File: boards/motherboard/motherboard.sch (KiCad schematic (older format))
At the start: 36 parts

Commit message: updates to mother board
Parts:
- 350ma1, 350ma10, 350ma11, 350ma12, 350ma13, 350ma14, 350ma15, 350ma2, 350ma3, 350ma4, 350ma5, 350ma6, 350ma7, 350ma8, 350ma9: renamed from 350ma?; footprint (none) -> lighting:350ma constant current xl4001
- J1, J2, J3, J4, J5: renamed from J?; footprint (none) -> lighting:RJ45
- R1, R10, R11, R12, R13, R14, R15, R2, R3, R4, R5, R6, R7, R8, R9: renamed from R?; footprint (none) -> Resistors_ThroughHole:Resistor_Horizontal_RM10mm
- U1: renamed from U?; footprint (none) -> lighting:pwm_pca9685
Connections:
- net GNDPWR: no longer 350ma14.5 (pwm), 350ma3.5 (pwm), 350ma5.5 (pwm), R14.2, R3.2, R5.2, U1.14 (LED13), U1.3 (LED2), U1.5 (LED4)
- net VCC: now also R11.1; no longer R11.2
- net led0: now also 350ma1.5 (pwm), R1.2
- net led1: no longer 350ma1.5 (pwm), R1.2
- net led10: now also R11.2; no longer R11.1
- new net led13: 350ma14.5 (pwm), R14.2, U1.14 (LED13)
- new net led2: 350ma3.5 (pwm), R3.2, U1.3 (LED2)
- new net led4: 350ma5.5 (pwm), R5.2, U1.5 (LED4)
- no-connect marks 3 -> 18
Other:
- moved on the sheet: 350ma10, 350ma11, 350ma12, 350ma13, 350ma14, 350ma15, 350ma4, 350ma7, 350ma8, 350ma9, J3, J4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

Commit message: mother board pcb
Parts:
- added P1: CONN_01X02, Pin_Headers:Pin_Header_Straight_1x02, symbol CONN_01X02
- added P2, P3: CONN_01X04, Pin_Headers:Pin_Header_Straight_1x04, symbol CONN_01X04
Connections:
- net +24V: now also P1.1 (P1); no longer 350ma9.5 (pwm), R9.2, U1.9 (LED8)
- net GND: now also P2.4 (P4), P3.4 (P4)
- net GNDPWR: now also P1.2 (P2)
- net VCC: now also P2.1 (P1), P3.1 (P1); no longer R12.1
- net sda: now reaches U1.19 (SDA), U1.25 (SDA)
- net sda: now also P2.2 (P2), P3.2 (P2)
- net scl: now reaches U1.20 (SCL), U1.26 (SCL)
- net scl: now also P2.3 (P3), P3.3 (P3)
- new net led8: 350ma9.5 (pwm), R9.2, U1.9 (LED8)
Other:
- moved on the sheet: 350ma1, 350ma10, R10, R12, R2
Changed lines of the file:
@@
 $EndComp
 $Comp
-L +24V #PWR01
+L +24V #PWR1
 U 1 1 5787E774
 P 8600 1350
-F 0 "#PWR01" H 8600 1200 50  0001 C CNN
+F 0 "#PWR1" H 8600 1200 50  0001 C CNN
 F 1 "+24V" H 8600 1490 50  0000 C CNN
 F 2 "" H 8600 1350 50  0000 C CNN
@@
 $EndComp
 $Comp
-L GNDPWR #PWR02
+L GNDPWR #PWR2
 U 1 1 5787E79E
 P 9150 1250
-F 0 "#PWR02" H 9150 1050 50  0001 C CNN
+F 0 "#PWR2" H 9150 1050 50  0001 C CNN
 F 1 "GNDPWR" H 9150 1120 50  0000 C CNN
 F 2 "" H 9150 1200 50  0000 C CNN
@@
 L Led_Driver 350ma1
 U 1 1 5787EC48
-P 5100 1700
-F 0 "350ma1" H 5100 1700 60  0000 C CNN
-F 1 "Led_Driver" H 5150 1800 60  0000 C CNN
-F 2 "lighting:350ma constant current xl4001" H 5100 1700 60  0001 C CNN
-F 3 "" H 5100 1700 60  0000 C CNN
-	1    5100 1700
+P 5050 1700
+F 0 "350ma1" H 5050 1700 60  0000 C CNN
+F 1 "Led_Driver" H 5100 1800 60  0000 C CNN
+F 2 "lighting:350ma constant current xl4001" H 5050 1700 60  0001 C CNN
+F 3 "" H 5050 1700 60  0000 C CNN
+	1    5050 1700
 	1    0    0    -1
 $EndComp
@@
 Text Label 5650 1050 0    60   ~ 0
 vpwr
-Text Label 5600 1200 0    60   ~ 0
-gndpwr
-Text Label 4600 1200 0    60   ~ 0
-vpwr
-Text Label 4600 1500 0    60   ~ 0
+Text Label 5550 1200 0    60   ~ 0
+gndpwr
+Text Label 4550 1200 0    60   ~ 0
+vpwr
+Text Label 4550 1500 0    60   ~ 0
 gnd
 Text Label 5650 1350 0    60   ~ 0
@@
 $EndComp
 $Comp
-L Led_Driver 350ma11
-U 1 1 5787FC55
-P 2600 3850
-F 0 "350ma11" H 2600 3850 60  0000 C CNN
-F 1 "Led_Driver" H 2650 3950 60  0000 C CNN
-F 2 "lighting:350ma constant current xl4001" H 2600 3850 60  0001 C CNN
-F 3 "" H 2600 3850 60  0000 C CNN
-	1    2600 3850
-	1    0    0    -1
-$EndComp
-$Comp
 L Led_Driver 350ma10
 U 1 1 5787FC5B
-P 1550 4000
-F 0 "350ma10" H 1550 4000 60  0000 C CNN
-F 1 "Led_Driver" H 1600 4100 60  0000 C CNN
-F 2 "lighting:350ma constant current xl4001" H 1550 4000 60  0001 C CNN
-F 3 "" H 1550 4000 60  0000 C CNN
-	1    1550 4000
+P 1250 4000
+F 0 "350ma10" H 1250 4000 60  0000 C CNN
+F 1 "Led_Driver" H 1300 4100 60  0000 C CNN
+F 2 "lighting:350ma constant current xl4001" H 1250 4000 60  0001 C CNN
+F 3 "" H 1250 4000 60  0000 C CNN
+	1    1250 4000
 	1    0    0    -1
 $EndComp
@@
 Text Label 2100 3350 0    60   ~ 0
 vpwr
-Text Label 2050 3500 0    60   ~ 0
-gndpwr
-Text Label 1050 3500 0    60   ~ 0
-vpwr
-Text Label 1050 3800 0    60   ~ 0
+Text Label 1750 3500 0    60   ~ 0
+gndpwr
+Text Label 750  3500 0    60   ~ 0
+vpwr
+Text Label 750  3800 0    60   ~ 0
 gnd
 Text Label 2100 3650 0    60   ~ 0
@@
 L R R2
 U 1 1 57881E5D
-P 5550 800
-F 0 "R2" V 5630 800 50  0000 C CNN
-F 1 "10k" V 5550 800 50  0000 C CNN
-F 2 "Resistors_ThroughHole:Resistor_Horizontal_RM10mm" V 5480 800 50  0001 C CNN
-F 3 "" H 5550 800 50  0000 C CNN
-	1    5550 800
-	1    0    0    -1
-$EndComp
-Text Label 5550 650  0    60   ~ 0
+P 5600 750
+F 0 "R2" V 5680 750 50  0000 C CNN
+F 1 "10k" V 5600 750 50  0000 C CNN
+F 2 "Resistors_ThroughHole:Resistor_Horizontal_RM10mm" V 5530 750 50  0001 C CNN
+F 3 "" H 5600 750 50  0000 C CNN
+	1    5600 750
+	1    0    0    -1
+$EndComp
+Text Label 5600 600  0    60   ~ 0
 vcc
 $Comp
@@
 L R R12
 U 1 1 5788238C
-P 3050 3100
-F 0 "R12" V 3130 3100 50  0000 C CNN
-F 1 "10k" V 3050 3100 50  0000 C CNN
-F 2 "Resistors_ThroughHole:Resistor_Horizontal_RM10mm" V 2980 3100 50  0001 C CNN
-F 3 "" H 3050 3100 50  0000 C CNN
-	1    3050 3100
+P 3150 3100
+F 0 "R12" V 3230 3100 50  0000 C CNN
+F 1 "10k" V 3150 3100 50  0000 C CNN
+F 2 "Resistors_ThroughHole:Resistor_Horizontal_RM10mm" V 3080 3100 50  0001 C CNN
+F 3 "" H 3150 3100 50  0000 C CNN
+	1    3150 3100
 	1    0    0    -1
 $EndComp
@@
 L R R10
 U 1 1 5788239A
-P 850 3400
-F 0 "R10" V 930 3400 50  0000 C CNN
-F 1 "10k" V 850 3400 50  0000 C CNN
-F 2 "Resistors_ThroughHole:Resistor_Horizontal_RM10mm" V 780 3400 50  0001 C CNN
-F 3 "" H 850 3400 50  0000 C CNN
-	1    850  3400
-	1    0    0    -1
-$EndComp
-Text Label 850  3250 0    60   ~ 0
+P 550 3400
+F 0 "R10" V 630 3400 50  0000 C CNN
+F 1 "10k" V 550 3400 50  0000 C CNN
+F 2 "Resistors_ThroughHole:Resistor_Horizontal_RM10mm" V 480 3400 50  0001 C CNN
+F 3 "" H 550 3400 50  0000 C CNN
+	1    550  3400
+	1    0    0    -1
+$EndComp
+Text Label 550  3250 0    60   ~ 0
 vcc
 $Comp
@@
 	2850 5200 2850 5150
 Wire Wire Line
-	1050 5200 2850 5200
-Wire Wire Line
-	1050 4100 1050 5200
+	750  5200 2850 5200
+Wire Wire Line
+	750  4100 750  5200
 Wire Wire Line
 	2050 5150 2750 5150
@@
 	6400 2900 6400 2850
 Wire Wire Line
-	4600 2900 6400 2900
-Wire Wire Line
-	4600 1800 4600 2900
-Wire Wire Line
-	5600 2850 6300 2850
-Wire Wire Line
-	5600 1800 5600 2850
-Wire Wire Line
-	7100 3450 7100 3900
+	4550 2900 6400 2900
+Wire Wire Line
+	5550 2850 6300 2850
 Wire Wire Line
 	5850 3450 5850 3750
@@
 	1950 3550 2100 3550
 Wire Wire Line
-	850  3550 850  3700
-Wire Wire Line
-	850  3700 1050 3700
+	550  3550 550  3700
+Wire Wire Line
+	550  3700 750  3700
 Wire Wire Line
 	3250 5700 3250 6150
@@
 	800  6150 850  6150
 Wire Wire Line
-	5550 950  5550 1250
-Wire Wire Line
-	5550 1250 5650 1250
-Wire Wire Line
 	4500 950  4500 1400
-Wire Wire Line
-	4500 1400 4600 1400
 Wire Wire Line
 	3100 950  3100 1400
@@
 Text Label 4500 950  0    60   ~ 0
 led0
-Text Label 5550 950  0    60   ~ 0
+Text Label 5600 900  0    60   ~ 0
 led1
 Text Label 800  950  0    60   ~ 0
@@
 Text Label 5850 3450 0    60   ~ 0
 led7
-Text Label 850  3550 0    60   ~ 0
+Text Label 550  3550 0    60   ~ 0
 led9
 Text Label 1950 3550 0    60   ~ 0
 led10
-Text Label 3050 3250 0    60   ~ 0
+Text Label 3150 3250 0    60   ~ 0
 led11
 Text Label 800  5700 0    60   ~ 0
@@
 NoConn ~ 10350 2350
 Wire Wire Line
-	3050 3250 3050 3700
-Wire Wire Line
-	3050 3700 3200 3700
-Wire Wire Line
 	1950 3350 1950 3550
 NoConn ~ 7200 2050
@@
 NoConn ~ 3400 7600
 $Comp
-L GND #PWR03
+L GND #PWR4
 U 1 1 57888F25
 P 10100 1550
-F 0 "#PWR03" H 10100 1300 50  0001 C CNN
+F 0 "#PWR4" H 10100 1300 50  0001 C CNN
 F 1 "GND" H 10100 1400 50  0000 C CNN
 F 2 "" H 10100 1550 50  0000 C CNN
@@
 $EndComp
 $Comp
-L VCC #PWR04
+L VCC #PWR3
 U 1 1 57888F81
 P 9800 1550
-F 0 "#PWR04" H 9800 1400 50  0001 C CNN
+F 0 "#PWR3" H 9800 1400 50  0001 C CNN
 F 1 "VCC" H 9800 1700 50  0000 C CNN
 F 2 "" H 9800 1550 50  0000 C CNN
@@
 Wire Wire Line
 	6700 950  6650 950
+Wire Wire Line
+	2050 4100 1750 4100
+$Comp
+L Led_Driver 350ma11
+U 1 1 5787FC55
+P 2600 3850
+F 0 "350ma11" H 2600 3850 60  0000 C CNN
+F 1 "Led_Driver" H 2650 3950 60  0000 C CNN
+F 2 "lighting:350ma constant current xl4001" H 2600 3850 60  0001 C CNN
+F 3 "" H 2600 3850 60  0000 C CNN
+	1    2600 3850
+	1    0    0    -1
+$EndComp
+Wire Wire Line
+	3150 3250 3150 3700
+Wire Wire Line
+	3150 3700 3200 3700
+Wire Wire Line
+	5600 900  5600 1250
+Wire Wire Line
+	5600 1250 5650 1250
+Wire Wire Line
+	4500 1400 4550 1400
+Wire Wire Line
+	5550 1800 5550 2850
+Wire Wire Line
+	4550 1800 4550 2900
+Wire Wire Line
+	7100 3450 7100 3600
+Wire Wire Line
+	7100 3600 7050 3600
+Wire Wire Line
+	7050 3600 7050 3900
+Wire Wire Line
+	7050 3900 7100 3900
+$Comp
+L CONN_01X04 P2
+U 1 1 578839F0
+P 10350 3900
+F 0 "P2" H 10350 4150 50  0000 C CNN
+F 1 "CONN_01X04" V 10450 3900 50  0000 C CNN
+F 2 "Pin_Headers:Pin_Header_Straight_1x04" H 10350 3900 50  0000 C CNN
+F 3 "" H 10350 3900 50  0000 C CNN
+	1    10350 3900
+	1    0    0    -1
+$EndComp
+$Comp
+L CONN_01X04 P3
+U 1 1 57883A8C
+P 10350 4550
+F 0 "P3" H 10350 4800 50  0000 C CNN
+F 1 "CONN_01X04" V 10450 4550 50  0000 C CNN
+F 2 "Pin_Headers:Pin_Header_Straight_1x04" H 10350 4550 50  0000 C CNN
+F 3 "" H 10350 4550 50  0000 C CNN
+	1    10350 4550
+	1    0    0    -1
+$EndComp
+$Comp
+L CONN_01X02 P1
+U 1 1 57883AF1
+P 10200 1000
+F 0 "P1" H 10200 1150 50  0000 C CNN
+F 1 "CONN_01X02" V 10300 1000 50  0000 C CNN
+F 2 "Pin_Headers:Pin_Header_Straight_1x02" H 10200 1000 50  0000 C CNN
+F 3 "" H 10200 1000 50  0000 C CNN
+	1    10200 1000
+	1    0    0    -1
+$EndComp
+Text Label 10000 950  0    60   ~ 0
+vpwr
+Text Label 10000 1050 0    60   ~ 0
+gndpwr
+Text Label 10150 3750 0    60   ~ 0
+vcc
+Text Label 10150 4400 0    60   ~ 0
+vcc
+Text Label 10150 3850 0    60   ~ 0
+sda
+Text Label 10150 4500 0    60   ~ 0
+sda
+Text Label 10350 2550 0    60   ~ 0
+sda
+Text Label 10350 2450 0    60   ~ 0
+scl
+Text Label 10150 3950 0    60   ~ 0
+scl
+Text Label 10150 4600 0    60   ~ 0
+scl
+Text Label 10150 4050 0    60   ~ 0
+gnd
+Text Label 10150 4700 0    60   ~ 0
+gnd
 $EndSCHEMATC

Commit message: before autoroute
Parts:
- J1, J2, J3, J4, J5: footprint lighting:RJ45 -> Connect:RJ45_8
- P1: footprint Pin_Headers:Pin_Header_Straight_1x02 -> lighting:TerminalBlock
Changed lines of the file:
@@
 F 0 "J1" H 6850 2900 50  0000 C CNN
 F 1 "RJ45" H 6500 2900 50  0000 C CNN
-F 2 "lighting:RJ45" H 6650 2400 50  0001 C CNN
+F 2 "Connect:RJ45_8" H 6650 2400 50  0001 C CNN
 F 3 "" H 6650 2400 50  0000 C CNN
 	1    6650 2400
@@
 F 0 "J4" H 7200 5400 50  0000 C CNN
 F 1 "RJ45" H 6850 5400 50  0000 C CNN
-F 2 "lighting:RJ45" H 7000 4900 50  0001 C CNN
+F 2 "Connect:RJ45_8" H 7000 4900 50  0001 C CNN
 F 3 "" H 7000 4900 50  0000 C CNN
 	1    7000 4900
@@
 F 0 "J2" H 3250 2900 50  0000 C CNN
 F 1 "RJ45" H 2900 2900 50  0000 C CNN
-F 2 "lighting:RJ45" H 3050 2400 50  0001 C CNN
+F 2 "Connect:RJ45_8" H 3050 2400 50  0001 C CNN
 F 3 "" H 3050 2400 50  0000 C CNN
 	1    3050 2400
@@
 F 0 "J3" H 3300 5200 50  0000 C CNN
 F 1 "RJ45" H 2950 5200 50  0000 C CNN
-F 2 "lighting:RJ45" H 3100 4700 50  0001 C CNN
+F 2 "Connect:RJ45_8" H 3100 4700 50  0001 C CNN
 F 3 "" H 3100 4700 50  0000 C CNN
 	1    3100 4700
@@
 F 0 "J5" H 3250 7650 50  0000 C CNN
 F 1 "RJ45" H 2900 7650 50  0000 C CNN
-F 2 "lighting:RJ45" H 3050 7150 50  0001 C CNN
+F 2 "Connect:RJ45_8" H 3050 7150 50  0001 C CNN
 F 3 "" H 3050 7150 50  0000 C CNN
 	1    3050 7150
@@
 F 0 "P1" H 10200 1150 50  0000 C CNN
 F 1 "CONN_01X02" V 10300 1000 50  0000 C CNN
-F 2 "Pin_Headers:Pin_Header_Straight_1x02" H 10200 1000 50  0000 C CNN
+F 2 "lighting:TerminalBlock" H 10200 1000 50  0000 C CNN
 F 3 "" H 10200 1000 50  0000 C CNN
 	1    10200 1000

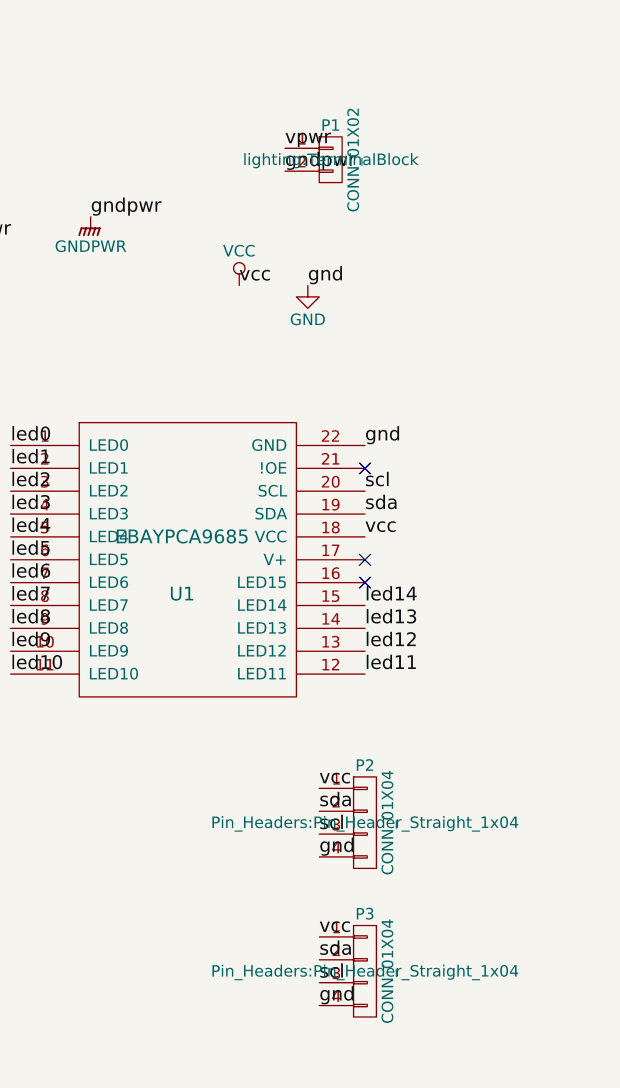
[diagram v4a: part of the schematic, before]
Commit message: added zones
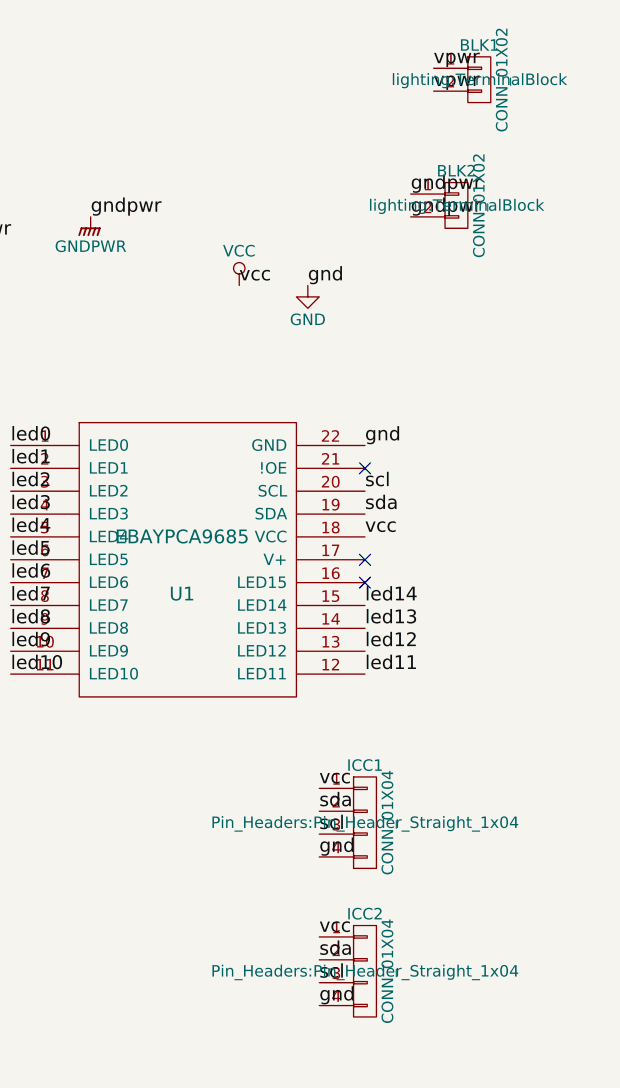
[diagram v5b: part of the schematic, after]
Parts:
- added BLK2: CONN_01X02, lighting:TerminalBlock, symbol CONN_01X02
- 350ma1, 350ma10, 350ma11, 350ma12, 350ma13, 350ma14, 350ma15, 350ma2, 350ma3, 350ma4, 350ma5, 350ma6, 350ma7, 350ma8, 350ma9: footprint lighting:350ma constant current xl4001 -> lighting:350ma_constant_current_xl4001
- renumbered P1 to BLK1, P2 to ICC1, P3 to ICC2
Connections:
- net +24V: now also BLK1.2 (P2)
- net GNDPWR: now also BLK2.1 (P1), BLK2.2 (P2); no longer BLK1.2 (P2)
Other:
- moved on the sheet: BLK1
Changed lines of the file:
@@
 F 0 "350ma3" H 7250 1700 60  0000 C CNN
 F 1 "Led_Driver" H 7300 1800 60  0000 C CNN
-F 2 "lighting:350ma constant current xl4001" H 7250 1700 60  0001 C CNN
+F 2 "lighting:350ma_constant_current_xl4001" H 7250 1700 60  0001 C CNN
 F 3 "" H 7250 1700 60  0000 C CNN
 	1    7250 1700
@@
 F 0 "350ma2" H 6150 1550 60  0000 C CNN
 F 1 "Led_Driver" H 6200 1650 60  0000 C CNN
-F 2 "lighting:350ma constant current xl4001" H 6150 1550 60  0001 C CNN
+F 2 "lighting:350ma_constant_current_xl4001" H 6150 1550 60  0001 C CNN
 F 3 "" H 6150 1550 60  0000 C CNN
 	1    6150 1550
@@
 F 0 "350ma1" H 5050 1700 60  0000 C CNN
 F 1 "Led_Driver" H 5100 1800 60  0000 C CNN
-F 2 "lighting:350ma constant current xl4001" H 5050 1700 60  0001 C CNN
+F 2 "lighting:350ma_constant_current_xl4001" H 5050 1700 60  0001 C CNN
 F 3 "" H 5050 1700 60  0000 C CNN
 	1    5050 1700
@@
 F 0 "350ma9" H 7600 4200 60  0000 C CNN
 F 1 "Led_Driver" H 7650 4300 60  0000 C CNN
-F 2 "lighting:350ma constant current xl4001" H 7600 4200 60  0001 C CNN
+F 2 "lighting:350ma_constant_current_xl4001" H 7600 4200 60  0001 C CNN
 F 3 "" H 7600 4200 60  0000 C CNN
 	1    7600 4200
@@
 F 0 "350ma8" H 6500 4050 60  0000 C CNN
 F 1 "Led_Driver" H 6550 4150 60  0000 C CNN
-F 2 "lighting:350ma constant current xl4001" H 6500 4050 60  0001 C CNN
+F 2 "lighting:350ma_constant_current_xl4001" H 6500 4050 60  0001 C CNN
 F 3 "" H 6500 4050 60  0000 C CNN
 	1    6500 4050
@@
 F 0 "350ma7" H 5250 4200 60  0000 C CNN
 F 1 "Led_Driver" H 5300 4300 60  0000 C CNN
-F 2 "lighting:350ma constant current xl4001" H 5250 4200 60  0001 C CNN
+F 2 "lighting:350ma_constant_current_xl4001" H 5250 4200 60  0001 C CNN
 F 3 "" H 5250 4200 60  0000 C CNN
 	1    5250 4200
@@
 F 0 "350ma6" H 3650 1700 60  0000 C CNN
 F 1 "Led_Driver" H 3700 1800 60  0000 C CNN
-F 2 "lighting:350ma constant current xl4001" H 3650 1700 60  0001 C CNN
+F 2 "lighting:350ma_constant_current_xl4001" H 3650 1700 60  0001 C CNN
 F 3 "" H 3650 1700 60  0000 C CNN
 	1    3650 1700
@@
 F 0 "350ma5" H 2550 1550 60  0000 C CNN
 F 1 "Led_Driver" H 2600 1650 60  0000 C CNN
-F 2 "lighting:350ma constant current xl4001" H 2550 1550 60  0001 C CNN
+F 2 "lighting:350ma_constant_current_xl4001" H 2550 1550 60  0001 C CNN
 F 3 "" H 2550 1550 60  0000 C CNN
 	1    2550 1550
@@
 F 0 "350ma4" H 1350 1700 60  0000 C CNN
 F 1 "Led_Driver" H 1400 1800 60  0000 C CNN
-F 2 "lighting:350ma constant current xl4001" H 1350 1700 60  0001 C CNN
+F 2 "lighting:350ma_constant_current_xl4001" H 1350 1700 60  0001 C CNN
 F 3 "" H 1350 1700 60  0000 C CNN
 	1    1350 1700
@@
 F 0 "350ma12" H 3700 4000 60  0000 C CNN
 F 1 "Led_Driver" H 3750 4100 60  0000 C CNN
-F 2 "lighting:350ma constant current xl4001" H 3700 4000 60  0001 C CNN
+F 2 "lighting:350ma_constant_current_xl4001" H 3700 4000 60  0001 C CNN
 F 3 "" H 3700 4000 60  0000 C CNN
 	1    3700 4000
@@
 F 0 "350ma10" H 1250 4000 60  0000 C CNN
 F 1 "Led_Driver" H 1300 4100 60  0000 C CNN
-F 2 "lighting:350ma constant current xl4001" H 1250 4000 60  0001 C CNN
+F 2 "lighting:350ma_constant_current_xl4001" H 1250 4000 60  0001 C CNN
 F 3 "" H 1250 4000 60  0000 C CNN
 	1    1250 4000
@@
 F 0 "350ma15" H 3900 6450 60  0000 C CNN
 F 1 "Led_Driver" H 3950 6550 60  0000 C CNN
-F 2 "lighting:350ma constant current xl4001" H 3900 6450 60  0001 C CNN
+F 2 "lighting:350ma_constant_current_xl4001" H 3900 6450 60  0001 C CNN
 F 3 "" H 3900 6450 60  0000 C CNN
 	1    3900 6450
@@
 F 0 "350ma14" H 2550 6300 60  0000 C CNN
 F 1 "Led_Driver" H 2600 6400 60  0000 C CNN
-F 2 "lighting:350ma constant current xl4001" H 2550 6300 60  0001 C CNN
+F 2 "lighting:350ma_constant_current_xl4001" H 2550 6300 60  0001 C CNN
 F 3 "" H 2550 6300 60  0000 C CNN
 	1    2550 6300
@@
 F 0 "350ma13" H 1350 6450 60  0000 C CNN
 F 1 "Led_Driver" H 1400 6550 60  0000 C CNN
-F 2 "lighting:350ma constant current xl4001" H 1350 6450 60  0001 C CNN
+F 2 "lighting:350ma_constant_current_xl4001" H 1350 6450 60  0001 C CNN
 F 3 "" H 1350 6450 60  0000 C CNN
 	1    1350 6450
@@
 F 0 "350ma11" H 2600 3850 60  0000 C CNN
 F 1 "Led_Driver" H 2650 3950 60  0000 C CNN
-F 2 "lighting:350ma constant current xl4001" H 2600 3850 60  0001 C CNN
+F 2 "lighting:350ma_constant_current_xl4001" H 2600 3850 60  0001 C CNN
 F 3 "" H 2600 3850 60  0000 C CNN
 	1    2600 3850
@@
 	7050 3900 7100 3900
 $Comp
-L CONN_01X04 P2
+L CONN_01X04 ICC1
 U 1 1 578839F0
 P 10350 3900
-F 0 "P2" H 10350 4150 50  0000 C CNN
+F 0 "ICC1" H 10350 4150 50  0000 C CNN
 F 1 "CONN_01X04" V 10450 3900 50  0000 C CNN
 F 2 "Pin_Headers:Pin_Header_Straight_1x04" H 10350 3900 50  0000 C CNN
@@
 $EndComp
 $Comp
-L CONN_01X04 P3
+L CONN_01X04 ICC2
 U 1 1 57883A8C
 P 10350 4550
-F 0 "P3" H 10350 4800 50  0000 C CNN
+F 0 "ICC2" H 10350 4800 50  0000 C CNN
 F 1 "CONN_01X04" V 10450 4550 50  0000 C CNN
 F 2 "Pin_Headers:Pin_Header_Straight_1x04" H 10350 4550 50  0000 C CNN
@@
 $EndComp
 $Comp
-L CONN_01X02 P1
+L CONN_01X02 BLK1
 U 1 1 57883AF1
-P 10200 1000
-F 0 "P1" H 10200 1150 50  0000 C CNN
-F 1 "CONN_01X02" V 10300 1000 50  0000 C CNN
-F 2 "lighting:TerminalBlock" H 10200 1000 50  0000 C CNN
-F 3 "" H 10200 1000 50  0000 C CNN
-	1    10200 1000
-	1    0    0    -1
-$EndComp
-Text Label 10000 950  0    60   ~ 0
-vpwr
-Text Label 10000 1050 0    60   ~ 0
+P 10850 650
+F 0 "BLK1" H 10850 800 50  0000 C CNN
+F 1 "CONN_01X02" V 10950 650 50  0000 C CNN
+F 2 "lighting:TerminalBlock" H 10850 650 50  0000 C CNN
+F 3 "" H 10850 650 50  0000 C CNN
+	1    10850 650
+	1    0    0    -1
+$EndComp
+Text Label 10650 600  0    60   ~ 0
+vpwr
+Text Label 10550 1150 0    60   ~ 0
 gndpwr
 Text Label 10150 3750 0    60   ~ 0
@@
 Text Label 10150 4700 0    60   ~ 0
 gnd
+$Comp
+L CONN_01X02 BLK2
+U 1 1 578D0231
+P 10750 1200
+F 0 "BLK2" H 10750 1350 50  0000 C CNN
+F 1 "CONN_01X02" V 10850 1200 50  0000 C CNN
+F 2 "lighting:TerminalBlock" H 10750 1200 50  0000 C CNN
+F 3 "" H 10750 1200 50  0000 C CNN
+	1    10750 1200
+	1    0    0    -1
+$EndComp
+Text Label 10650 700  0    60   ~ 0
+vpwr
+Text Label 10550 1250 0    60   ~ 0
+gndpwr
 $EndSCHEMATC

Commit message: another revision
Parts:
- BLK1, BLK2: footprint lighting:TerminalBlock -> Connect:bornier2
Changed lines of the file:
@@
 F 0 "BLK1" H 10850 800 50  0000 C CNN
 F 1 "CONN_01X02" V 10950 650 50  0000 C CNN
-F 2 "lighting:TerminalBlock" H 10850 650 50  0000 C CNN
+F 2 "Connect:bornier2" H 10850 650 50  0000 C CNN
 F 3 "" H 10850 650 50  0000 C CNN
 	1    10850 650
@@
 F 0 "BLK2" H 10750 1350 50  0000 C CNN
 F 1 "CONN_01X02" V 10850 1200 50  0000 C CNN
-F 2 "lighting:TerminalBlock" H 10750 1200 50  0000 C CNN
+F 2 "Connect:bornier2" H 10750 1200 50  0000 C CNN
 F 3 "" H 10750 1200 50  0000 C CNN
 	1    10750 1200

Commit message: minor fix
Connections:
- net VCC: now also R12.1
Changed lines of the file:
@@
 	1    0    0    -1
 $EndComp
-Text Label 3050 2950 0    60   ~ 0
+Text Label 3150 2950 0    60   ~ 0
 vcc
 $Comp
